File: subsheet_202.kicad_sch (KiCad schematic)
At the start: 15 parts, among them J203 DB-25S Parallel port, U202 YM2149_PHY

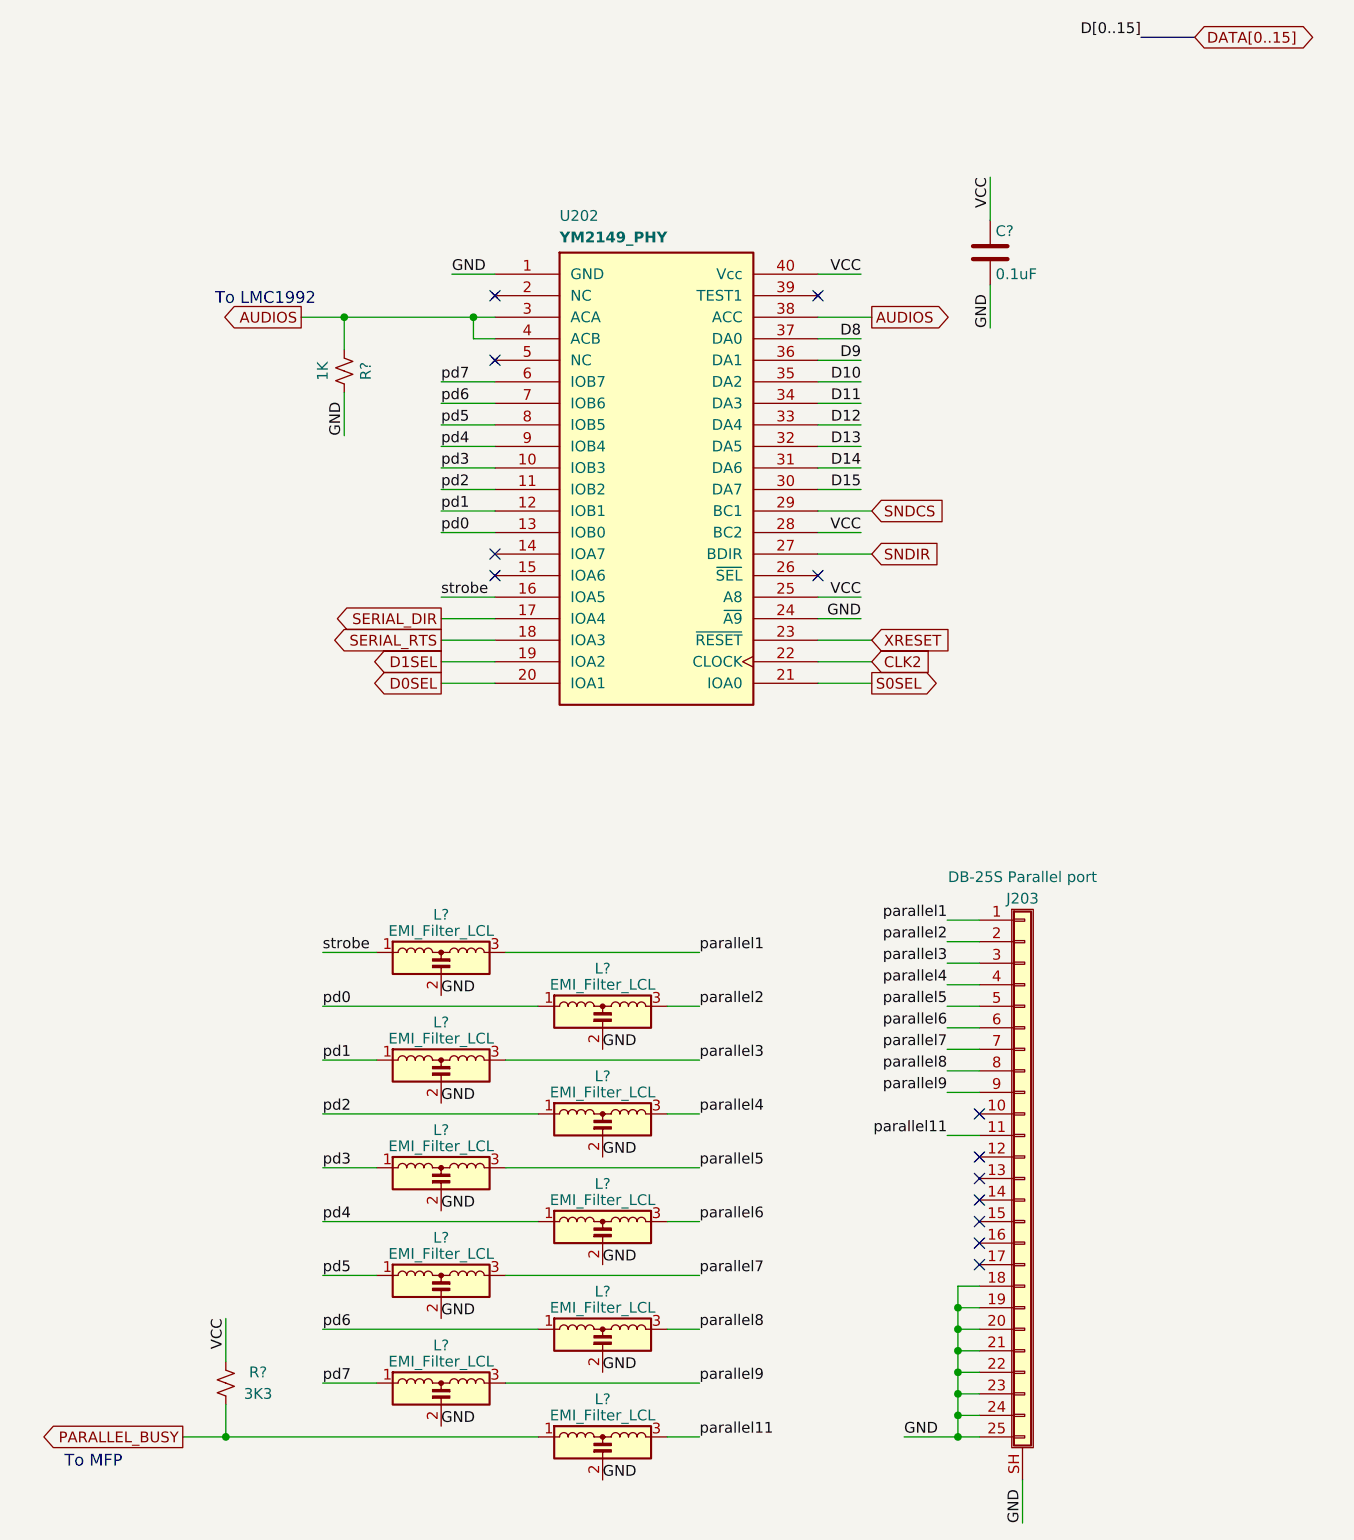
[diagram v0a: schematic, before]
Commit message: Resolves #3 : [schematic] annotate video port with signal name
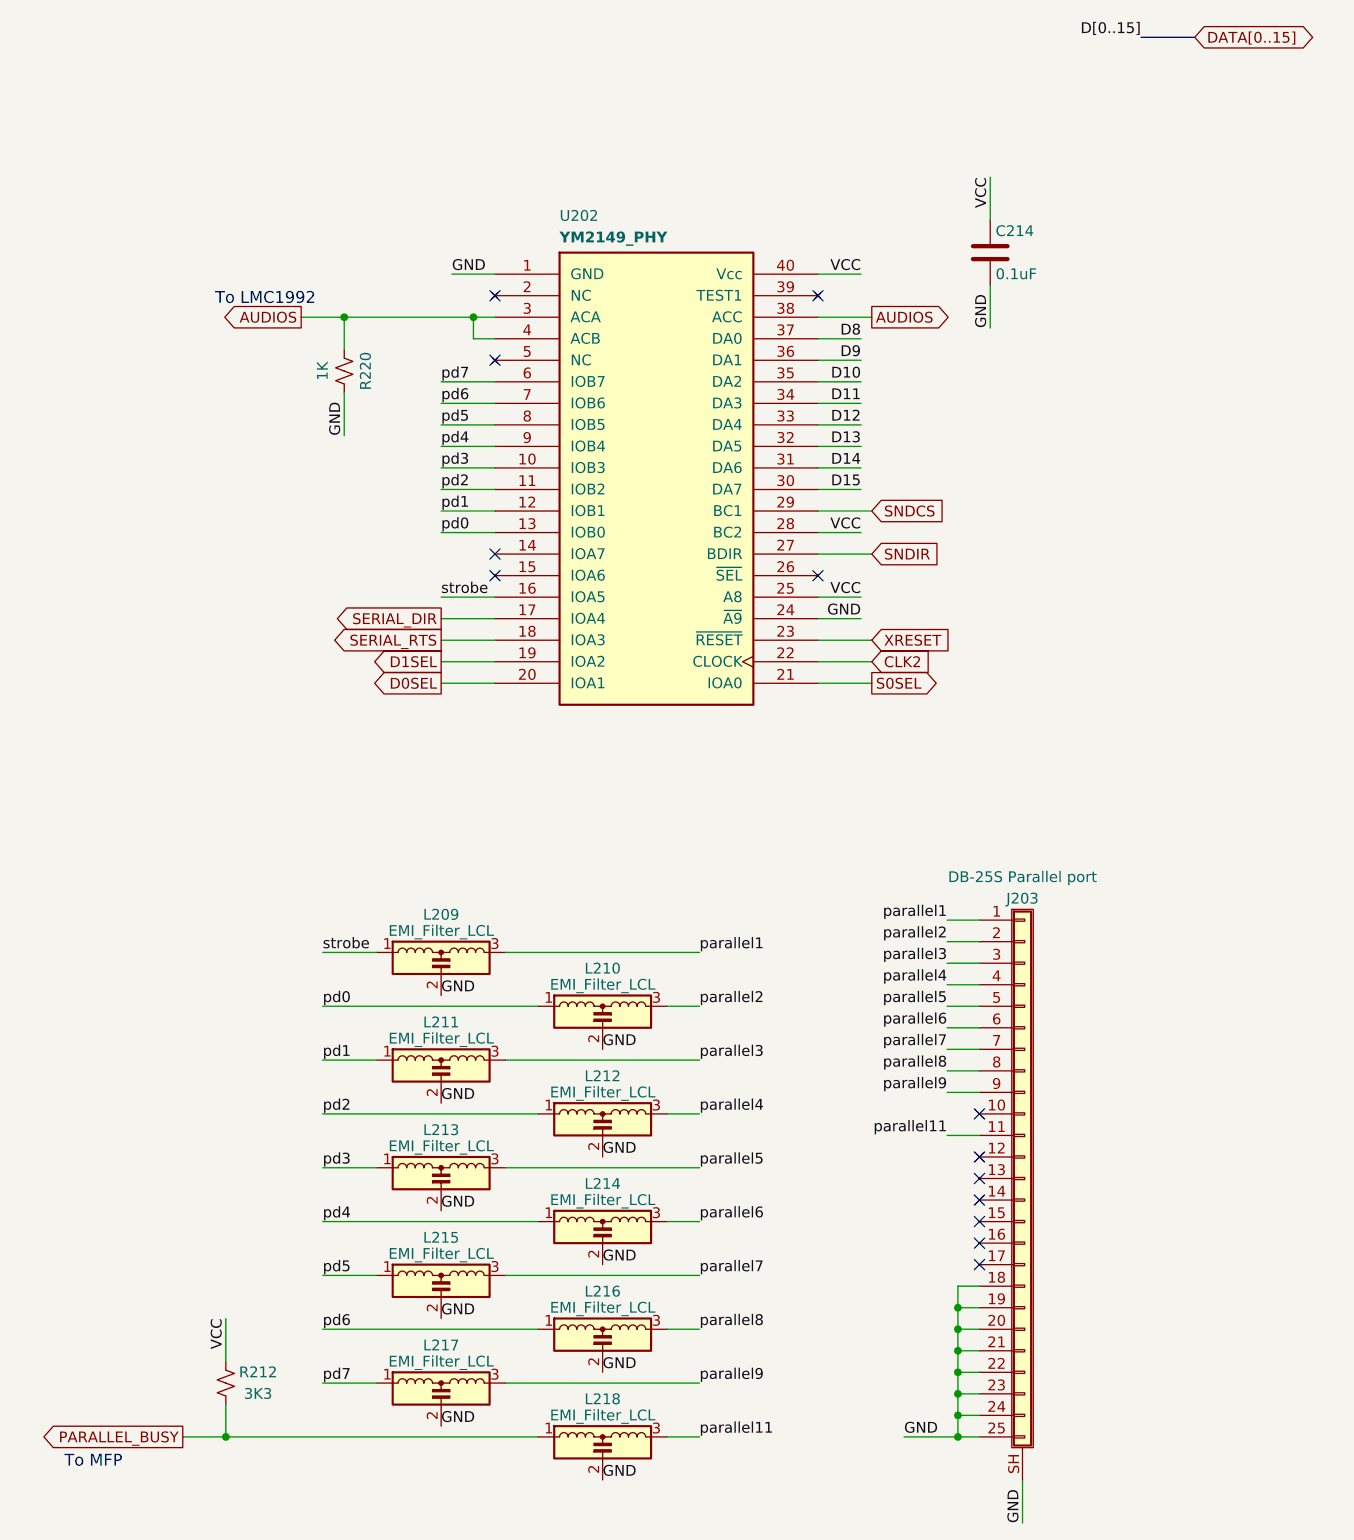
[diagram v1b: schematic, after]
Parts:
- gave numbers to parts that had none: 13
